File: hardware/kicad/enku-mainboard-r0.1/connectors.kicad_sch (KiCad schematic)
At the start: 15 parts

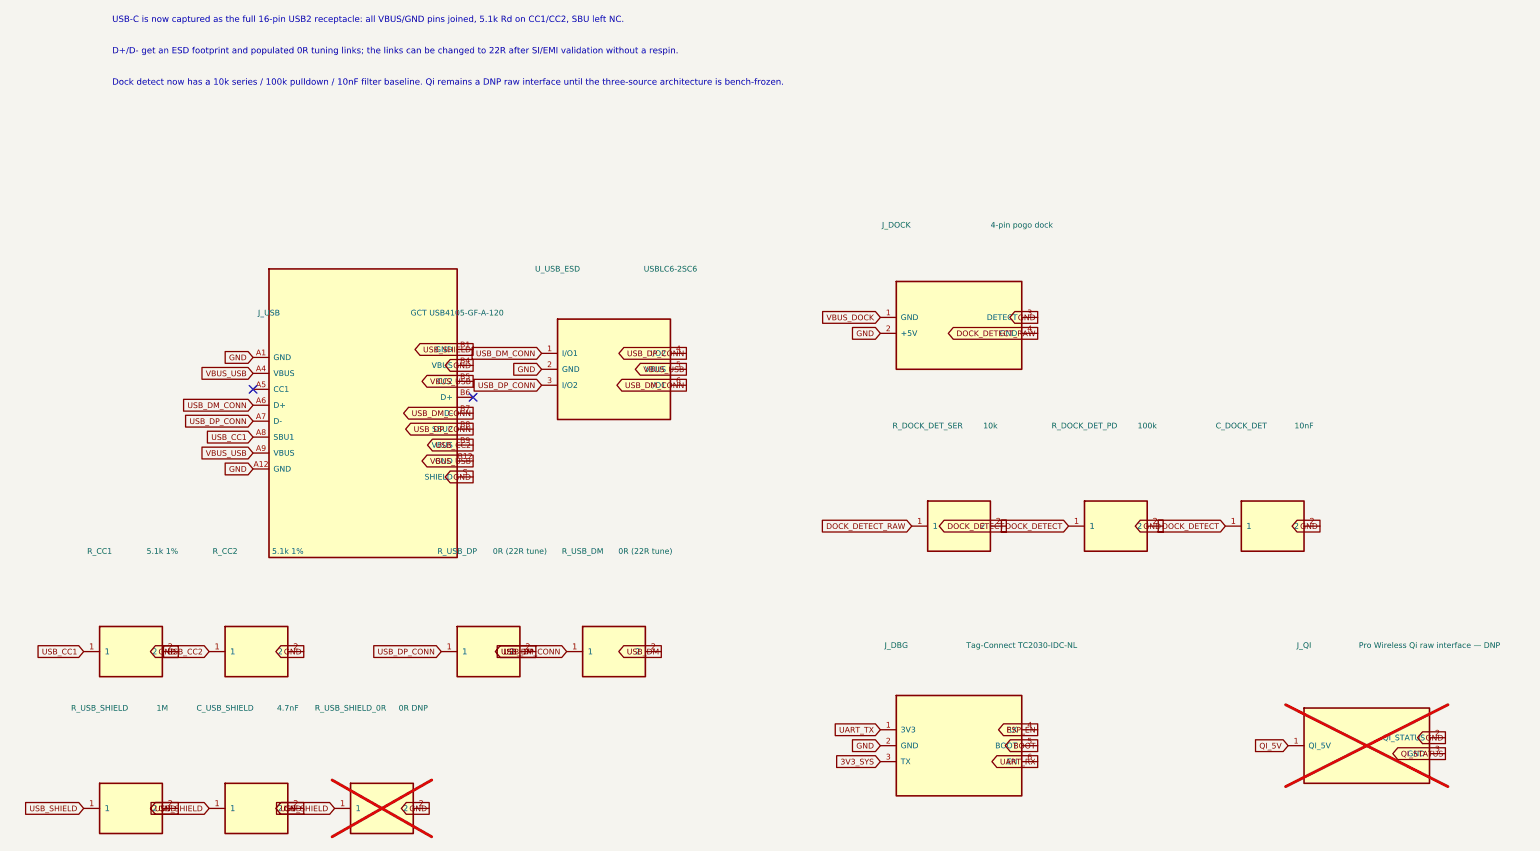
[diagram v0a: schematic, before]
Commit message: Fix KiCad pin-label Y transform in connectors
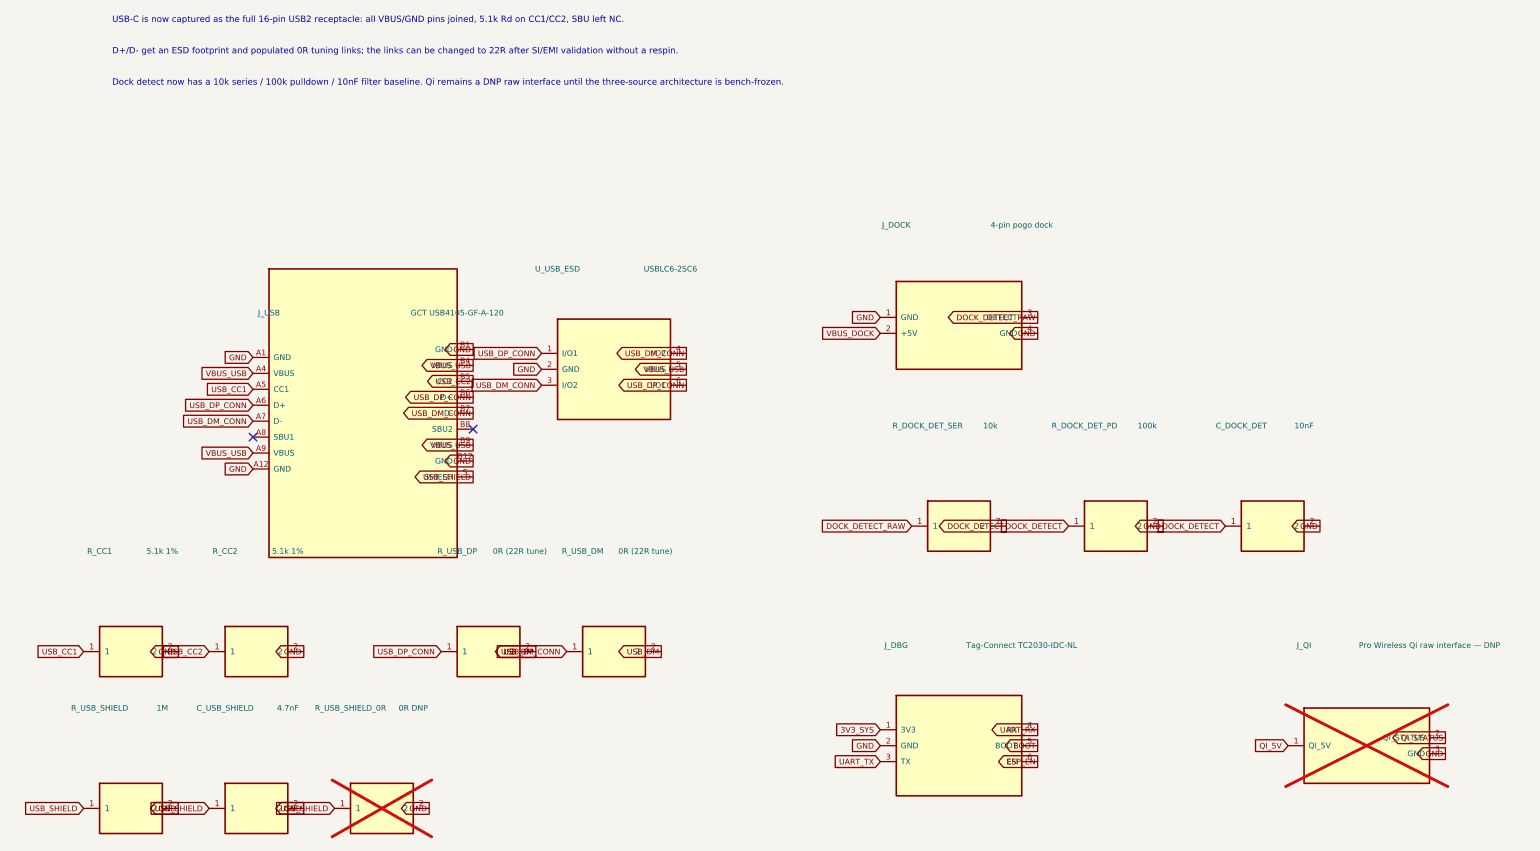
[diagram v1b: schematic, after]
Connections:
- net 3V3_SYS: now also J_DBG.1 (3V3); no longer J_DBG.3 (TX)
- net DOCK_DETECT_RAW: now also J_DOCK.3 (DETECT); no longer J_DOCK.4 (GND)
- net ESP_EN: now also J_DBG.6 (EN); no longer J_DBG.4 (RX)
- net GND: now also J_DOCK.1 (GND), J_DOCK.4 (GND), J_QI.3 (GND), J_USB.B1 (GND), J_USB.B12 (GND); no longer J_DOCK.2 (+5V), J_DOCK.3 (DETECT), J_QI.2 (QI_STATUS), J_USB.B4 (VBUS), J_USB.S (SHIELD)
- net QI_STATUS: now also J_QI.2 (QI_STATUS); no longer J_QI.3 (GND)
- net UART_RX: now also J_DBG.4 (RX); no longer J_DBG.6 (EN)
- net UART_TX: now also J_DBG.3 (TX); no longer J_DBG.1 (3V3)
- net USB_CC1: now also J_USB.A5 (CC1); no longer J_USB.A8 (SBU1)
- net USB_CC2: now also J_USB.B5 (CC2); no longer J_USB.B9 (VBUS)
- net USB_DM_CONN: now also J_USB.A7 (D-), U_USB_ESD.3 (I/O2), U_USB_ESD.4 (I/O2); no longer J_USB.A6 (D+), U_USB_ESD.1 (I/O1), U_USB_ESD.6 (I/O1)
- net USB_DP_CONN: now also J_USB.A6 (D+), J_USB.B6 (D+), U_USB_ESD.1 (I/O1), U_USB_ESD.6 (I/O1); no longer J_USB.A7 (D-), J_USB.B8 (SBU2), U_USB_ESD.3 (I/O2), U_USB_ESD.4 (I/O2)
- net USB_SHIELD: now also J_USB.S (SHIELD); no longer J_USB.B1 (GND)
- net VBUS_DOCK: now also J_DOCK.2 (+5V); no longer J_DOCK.1 (GND)
- net VBUS_USB: now also J_USB.B4 (VBUS), J_USB.B9 (VBUS); no longer J_USB.B12 (GND), J_USB.B5 (CC2)
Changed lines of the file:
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@@
 		(instances (project "enku-mainboard-r0.1" (path "/10000000-0000-4000-8000-000000000001/10000000-0000-4000-8000-000000000050" (reference "J_USB") (unit 1))))
 	)
+	(global_label "GND" (shape input) (at 47.46 73.11 0) (effects (font (size 0.9 0.9)) (justify right bottom)))
+	(global_label "VBUS_USB" (shape input) (at 47.46 75.65 0) (effects (font (size 0.9 0.9)) (justify right bottom)))
+	(global_label "USB_CC1" (shape input) (at 47.46 78.19 0) (effects (font (size 0.9 0.9)) (justify right bottom)))
+	(global_label "USB_DP_CONN" (shape input) (at 47.46 80.73 0) (effects (font (size 0.9 0.9)) (justify right bottom)))
+	(global_label "USB_DM_CONN" (shape input) (at 47.46 83.27 0) (effects (font (size 0.9 0.9)) (justify right bottom)))
+	(global_label "VBUS_USB" (shape input) (at 47.46 88.35 0) (effects (font (size 0.9 0.9)) (justify right bottom)))
 	(global_label "GND" (shape input) (at 47.46 90.89 0) (effects (font (size 0.9 0.9)) (justify right bottom)))
-	(global_label "VBUS_USB" (shape input) (at 47.46 88.35 0) (effects (font (size 0.9 0.9)) (justify right bottom)))
-	(global_label "USB_CC1" (shape input) (at 47.46 85.81 0) (effects (font (size 0.9 0.9)) (justify right bottom)))
-	(global_label "USB_DP_CONN" (shape input) (at 47.46 83.27 0) (effects (font (size 0.9 0.9)) (justify right bottom)))
-	(global_label "USB_DM_CONN" (shape input) (at 47.46 80.73 0) (effects (font (size 0.9 0.9)) (justify right bottom)))
-	(global_label "VBUS_USB" (shape input) (at 47.46 75.65 0) (effects (font (size 0.9 0.9)) (justify right bottom)))
-	(global_label "GND" (shape input) (at 47.46 73.11 0) (effects (font (size 0.9 0.9)) (justify right bottom)))
-	(global_label "GND" (shape output) (at 82.53999999999999 92.16 180) (effects (font (size 0.9 0.9)) (justify right bottom)))
-	(global_label "VBUS_USB" (shape output) (at 82.53999999999999 89.61999999999999 180) (effects (font (size 0.9 0.9)) (justify right bottom)))
-	(global_label "USB_CC2" (shape output) (at 82.53999999999999 87.08 180) (effects (font (size 0.9 0.9)) (justify right bottom)))
-	(global_label "USB_DP_CONN" (shape output) (at 82.53999999999999 84.53999999999999 180) (effects (font (size 0.9 0.9)) (justify right bottom)))
+	(global_label "GND" (shape output) (at 82.54 71.84 180) (effects (font (size 0.9 0.9)) (justify right bottom)))
+	(global_label "VBUS_USB" (shape output) (at 82.54 74.38 180) (effects (font (size 0.9 0.9)) (justify right bottom)))
+	(global_label "USB_CC2" (shape output) (at 82.54 76.92 180) (effects (font (size 0.9 0.9)) (justify right bottom)))
+	(global_label "USB_DP_CONN" (shape output) (at 82.54 79.46 180) (effects (font (size 0.9 0.9)) (justify right bottom)))
 	(global_label "USB_DM_CONN" (shape output) (at 82.53999999999999 82 180) (effects (font (size 0.9 0.9)) (justify right bottom)))
-	(global_label "VBUS_USB" (shape output) (at 82.53999999999999 76.92 180) (effects (font (size 0.9 0.9)) (justify right bottom)))
-	(global_label "GND" (shape output) (at 82.53999999999999 74.38 180) (effects (font (size 0.9 0.9)) (justify right bottom)))
-	(global_label "USB_SHIELD" (shape output) (at 82.53999999999999 71.84 180) (effects (font (size 0.9 0.9)) (justify right bottom)))
-	(no_connect (at 47.46 78.19))
-	(no_connect (at 82.53999999999999 79.46))
+	(global_label "VBUS_USB" (shape output) (at 82.54 87.08 180) (effects (font (size 0.9 0.9)) (justify right bottom)))
+	(global_label "GND" (shape output) (at 82.54 89.62 180) (effects (font (size 0.9 0.9)) (justify right bottom)))
+	(global_label "USB_SHIELD" (shape output) (at 82.54 92.16 180) (effects (font (size 0.9 0.9)) (justify right bottom)))
+	(no_connect (at 47.46 85.81))
+	(no_connect (at 82.54 84.54))
 	(symbol (lib_id "ENKU:R") (at 28 120 0) (unit 1) (exclude_from_sim no) (in_bom yes) (on_board yes) (dnp no)
 		(property "Reference" "R_CC1" (at 23 104 0) (effects (font (size 0.9 0.9))))
@@
 		(instances (project "enku-mainboard-r0.1" (path "/10000000-0000-4000-8000-000000000001/10000000-0000-4000-8000-000000000050" (reference "U_USB_ESD") (unit 1))))
 	)
-	(global_label "USB_DP_CONN" (shape input) (at 93.46000000000001 77.54 0) (effects (font (size 0.9 0.9)) (justify right bottom)))
+	(global_label "USB_DP_CONN" (shape input) (at 93.46 72.46 0) (effects (font (size 0.9 0.9)) (justify right bottom)))
 	(global_label "GND" (shape input) (at 93.46000000000001 75 0) (effects (font (size 0.9 0.9)) (justify right bottom)))
-	(global_label "USB_DM_CONN" (shape input) (at 93.46000000000001 72.46000000000001 0) (effects (font (size 0.9 0.9)) (justify right bottom)))
-	(global_label "USB_DM_CONN" (shape output) (at 116.53999999999999 77.54 180) (effects (font (size 0.9 0.9)) (justify right bottom)))
+	(global_label "USB_DM_CONN" (shape input) (at 93.46 77.54 0) (effects (font (size 0.9 0.9)) (justify right bottom)))
+	(global_label "USB_DM_CONN" (shape output) (at 116.54 72.46 180) (effects (font (size 0.9 0.9)) (justify right bottom)))
 	(global_label "VBUS_USB" (shape output) (at 116.53999999999999 75 180) (effects (font (size 0.9 0.9)) (justify right bottom)))
-	(global_label "USB_DP_CONN" (shape output) (at 116.53999999999999 72.46000000000001 180) (effects (font (size 0.9 0.9)) (justify right bottom)))
+	(global_label "USB_DP_CONN" (shape output) (at 116.54 77.54 180) (effects (font (size 0.9 0.9)) (justify right bottom)))
 	(symbol (lib_id "ENKU:R") (at 28 145 0) (unit 1) (exclude_from_sim no) (in_bom yes) (on_board yes) (dnp no)
 		(property "Reference" "R_USB_SHIELD" (at 23 129 0) (effects (font (size 0.9 0.9))))
@@
 		(instances (project "enku-mainboard-r0.1" (path "/10000000-0000-4000-8000-000000000001/10000000-0000-4000-8000-000000000050" (reference "J_DOCK") (unit 1))))
 	)
-	(global_label "GND" (shape input) (at 147.46 69.27 0) (effects (font (size 0.9 0.9)) (justify right bottom)))
-	(global_label "VBUS_DOCK" (shape input) (at 147.46 66.72999999999999 0) (effects (font (size 0.9 0.9)) (justify right bottom)))
-	(global_label "DOCK_DETECT_RAW" (shape output) (at 172.54 69.27 180) (effects (font (size 0.9 0.9)) (justify right bottom)))
-	(global_label "GND" (shape output) (at 172.54 66.72999999999999 180) (effects (font (size 0.9 0.9)) (justify right bottom)))
+	(global_label "GND" (shape input) (at 147.46 66.73 0) (effects (font (size 0.9 0.9)) (justify right bottom)))
+	(global_label "VBUS_DOCK" (shape input) (at 147.46 69.27 0) (effects (font (size 0.9 0.9)) (justify right bottom)))
+	(global_label "DOCK_DETECT_RAW" (shape output) (at 172.54 66.73 180) (effects (font (size 0.9 0.9)) (justify right bottom)))
+	(global_label "GND" (shape output) (at 172.54 69.27 180) (effects (font (size 0.9 0.9)) (justify right bottom)))
 	(symbol (lib_id "ENKU:R") (at 160 100 0) (unit 1) (exclude_from_sim no) (in_bom yes) (on_board yes) (dnp no)
 		(property "Reference" "R_DOCK_DET_SER" (at 155 84 0) (effects (font (size 0.9 0.9))))
@@
 		(instances (project "enku-mainboard-r0.1" (path "/10000000-0000-4000-8000-000000000001/10000000-0000-4000-8000-000000000050" (reference "J_DBG") (unit 1))))
 	)
-	(global_label "3V3_SYS" (shape input) (at 147.46 137.54 0) (effects (font (size 0.9 0.9)) (justify right bottom)))
+	(global_label "3V3_SYS" (shape input) (at 147.46 132.46 0) (effects (font (size 0.9 0.9)) (justify right bottom)))
 	(global_label "GND" (shape input) (at 147.46 135 0) (effects (font (size 0.9 0.9)) (justify right bottom)))
-	(global_label "UART_TX" (shape input) (at 147.46 132.45999999999998 0) (effects (font (size 0.9 0.9)) (justify right bottom)))
-	(global_label "UART_RX" (shape output) (at 172.54 137.54 180) (effects (font (size 0.9 0.9)) (justify right bottom)))
+	(global_label "UART_TX" (shape input) (at 147.46 137.54 0) (effects (font (size 0.9 0.9)) (justify right bottom)))
+	(global_label "UART_RX" (shape output) (at 172.54 132.46 180) (effects (font (size 0.9 0.9)) (justify right bottom)))
 	(global_label "BOOT" (shape output) (at 172.54 135 180) (effects (font (size 0.9 0.9)) (justify right bottom)))
-	(global_label "ESP_EN" (shape output) (at 172.54 132.45999999999998 180) (effects (font (size 0.9 0.9)) (justify right bottom)))
+	(global_label "ESP_EN" (shape output) (at 172.54 137.54 180) (effects (font (size 0.9 0.9)) (justify right bottom)))
 	(symbol (lib_id "ENKU:QI3") (at 225 135 0) (unit 1) (exclude_from_sim no) (in_bom yes) (on_board yes) (dnp yes)
 		(property "Reference" "J_QI" (at 215 119 0) (effects (font (size 0.9 0.9))))
@@
 	)
 	(global_label "QI_5V" (shape input) (at 212.46 135 0) (effects (font (size 0.9 0.9)) (justify right bottom)))
-	(global_label "QI_STATUS" (shape output) (at 237.54 136.27 180) (effects (font (size 0.9 0.9)) (justify right bottom)))
-	(global_label "GND" (shape output) (at 237.54 133.73000000000002 180) (effects (font (size 0.9 0.9)) (justify right bottom)))
+	(global_label "QI_STATUS" (shape output) (at 237.54 133.73 180) (effects (font (size 0.9 0.9)) (justify right bottom)))
+	(global_label "GND" (shape output) (at 237.54 136.27 180) (effects (font (size 0.9 0.9)) (justify right bottom)))
 	(text "USB-C is now captured as the full 16-pin USB2 receptacle: all VBUS/GND pins joined, 5.1k Rd on CC1/CC2, SBU left NC." (exclude_from_sim no) (at 25 20 0) (effects (font (size 1.0 1.0)) (justify left bottom)))
 	(text "D+/D- get an ESD footprint and populated 0R tuning links; the links can be changed to 22R after SI/EMI validation without a respin." (exclude_from_sim no) (at 25 25 0) (effects (font (size 1.0 1.0)) (justify left bottom)))
